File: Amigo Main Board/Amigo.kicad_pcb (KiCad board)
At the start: 2 copper layers, 75.5 x 75 mm, 39 parts, among them J1 USB_C_Receptacle_USB2.0_16P, J2 Conn_01x02, J3 SH1106 OLED, J4 MAX98357A, J5 DRV8833, J6 ButtonRibbonConnector, SW1 SW_Push, SW2 SW_Push, U1 TP4056-42-ESOP8, U2 AP2112K-3.3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

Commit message: Main PCB placement
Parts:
- added REF**: MountingHole_3.2mm_M3, MountingHole:MountingHole_3.2mm_M3, F.Cu at (15.5, 58.5)
- added REF**: MountingHole_3.2mm_M3, MountingHole:MountingHole_3.2mm_M3, F.Cu at (58.5, 15.5)
- added REF**: MountingHole_3.2mm_M3, MountingHole:MountingHole_3.2mm_M3, F.Cu at (58.5, 58.5)
- added REF**: MountingHole_3.2mm_M3, MountingHole:MountingHole_3.2mm_M3, F.Cu at (15.5, 15.5)
- moved J3 188.8 mm to (21.0, 21.7)
- moved R8 184.1 mm to (18.0, 22.5), turned to 90 degrees
- moved R9 183.7 mm to (18.0, 26.2), turned to 90 degrees
- moved J4 182.2 mm to (14.5, 22.0)
- moved C11 176.6 mm to (14.5, 41.5), turned to -90 degrees
- moved C13 175.5 mm to (24.5, 22.5), turned to -90 degrees
- moved C10 175.0 mm to (14.6, 46.0), turned to 90 degrees
- moved C12 172.2 mm to (24.5, 26.0), turned to -90 degrees
- moved U2 168.3 mm to (31.5, 22.0), turned to 180 degrees
- moved D2 168.2 mm to (37.0, 49.5)
- moved D1 166.3 mm to (37.0, 52.2)
- moved J1 165.0 mm to (22.2, 56.0)
- moved R1 164.9 mm to (25.0, 53.0)
- moved J5 164.7 mm to (27.5, 21.8)
- moved D3 164.1 mm to (56.8, 21.6), turned to 180 degrees
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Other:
- board size 75.5 x 75 mm -> 50 x 50 mm

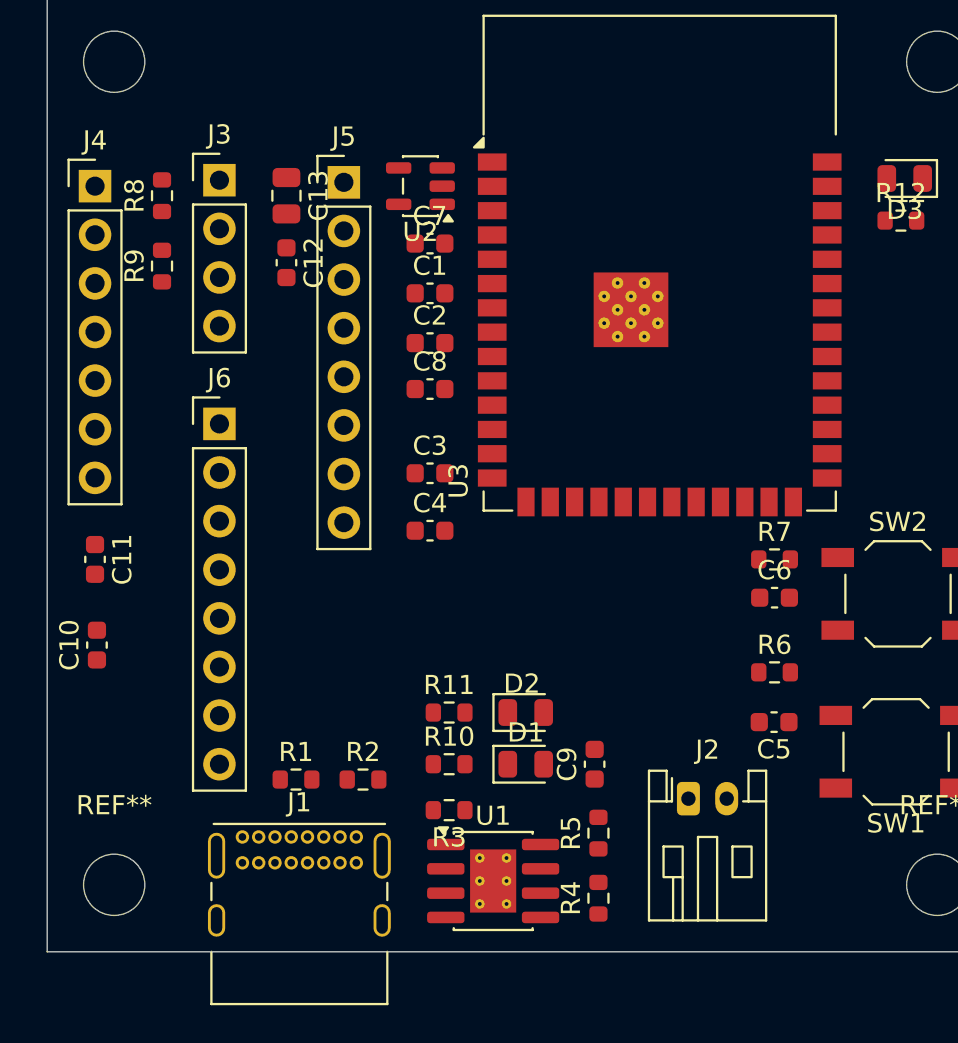
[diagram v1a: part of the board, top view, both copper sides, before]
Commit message: PCB wiring done
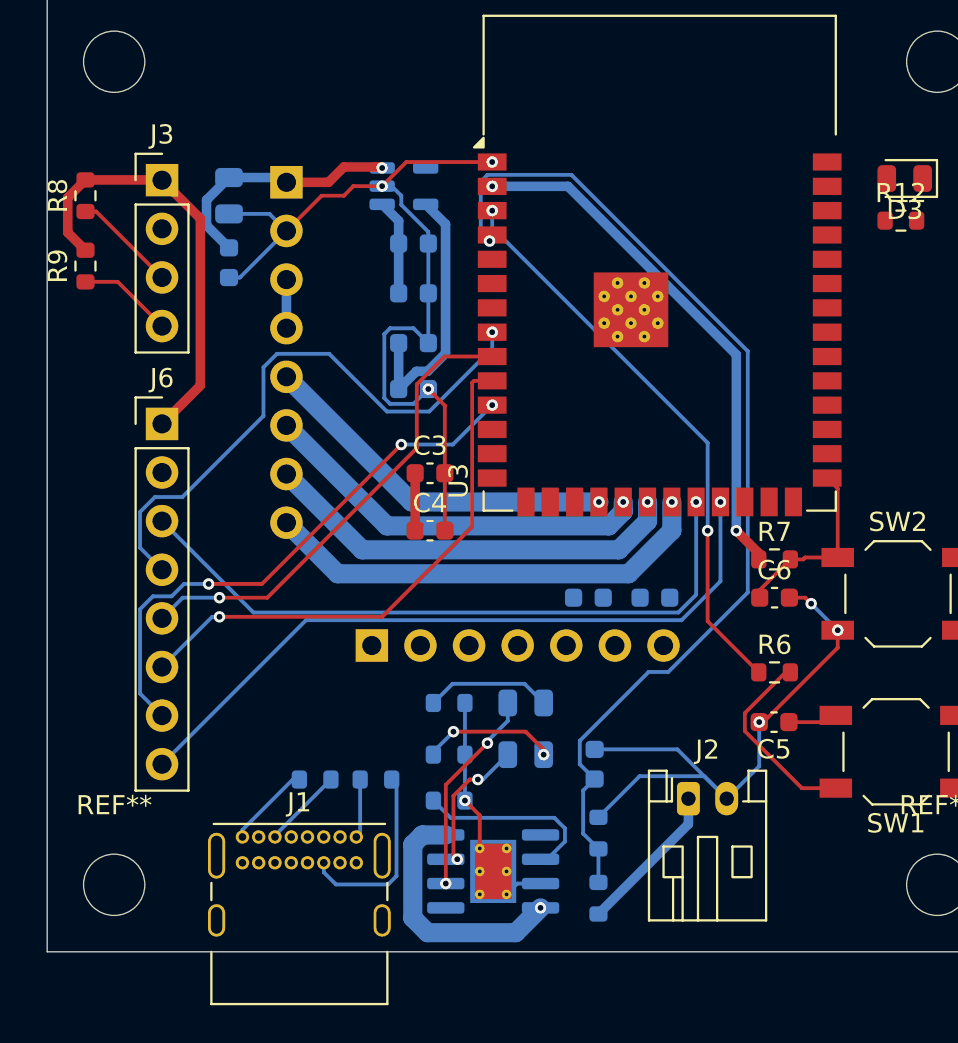
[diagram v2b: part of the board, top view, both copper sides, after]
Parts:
- C1, C10, C11, C12, C13, C2, C7, C8, C9, D1, D2, J4, J5, R1, R10, R11, R2, R3, R4, R5, U1, U2: moved to B.Cu
- moved C11 29.3 mm to (43.8, 43.5), turned to 0 degrees
- moved J4 28.0 mm to (29.0, 46.0), turned to -90 degrees
- moved C10 25.8 mm to (40.3, 43.5), turned to 180 degrees
- moved R8 4.00 mm to (14.0, 22.5)
- moved R9 4.00 mm to (14.0, 26.2)
- moved C12 3.00 mm to (21.5, 26.0)
- moved C13 3.00 mm to (21.5, 22.5)
- moved J3 3.00 mm to (18.0, 21.7)
- moved J5 3.00 mm to (24.5, 21.8), turned to 180 degrees
- moved J6 3.00 mm to (18.0, 34.4)
- moved R1 1.00 mm to (26.0, 53.0), turned to 180 degrees
- moved C1 0.86 mm to (31.1, 27.6)
- moved C2 0.86 mm to (31.1, 30.2)
- moved C7 0.86 mm to (31.1, 25.0)
- moved C8 0.86 mm to (31.1, 32.6)
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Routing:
- net GND: track 0.00 -> 93.8 mm, vias 0 -> 7
- net +3V3: track 0.00 -> 69.8 mm, vias 0 -> 2
- net BAT_SENSE: track 0.00 -> 54.1 mm, vias 0 -> 1
- net BUTTON_COL_2: track 0.00 -> 37.3 mm, vias 0 -> 1
- net BUTTON_ROW_0: track 0.00 -> 35.1 mm, vias 0 -> 1
- net BUTTON_ROW_1: track 0.00 -> 30.3 mm, vias 0 -> 1
- net EN: track 0.00 -> 29.9 mm, vias 0 -> 2
- net BUTTON_COL_1: track 0.00 -> 28.8 mm, vias 0 -> 3
- net BUTTON_COL_0: track 0.00 -> 27.9 mm, vias 0 -> 1
- net BAT+: track 0.00 -> 26.1 mm, vias 0 -> 1
- net BUTTON_ROW_2: track 0.00 -> 24.9 mm, vias 0 -> 1
- net MOTOR_B_IN2: track 0.00 -> 23.7 mm, vias 0 -> 1
- net MOTOR_B_IN1: track 0.00 -> 22.1 mm, vias 0 -> 1
- net MOTOR_A_IN2: track 0.00 -> 20.6 mm, vias 0 -> 1
- net MOTOR_A_IN1: track 0.00 -> 19.0 mm, vias 0 -> 1
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
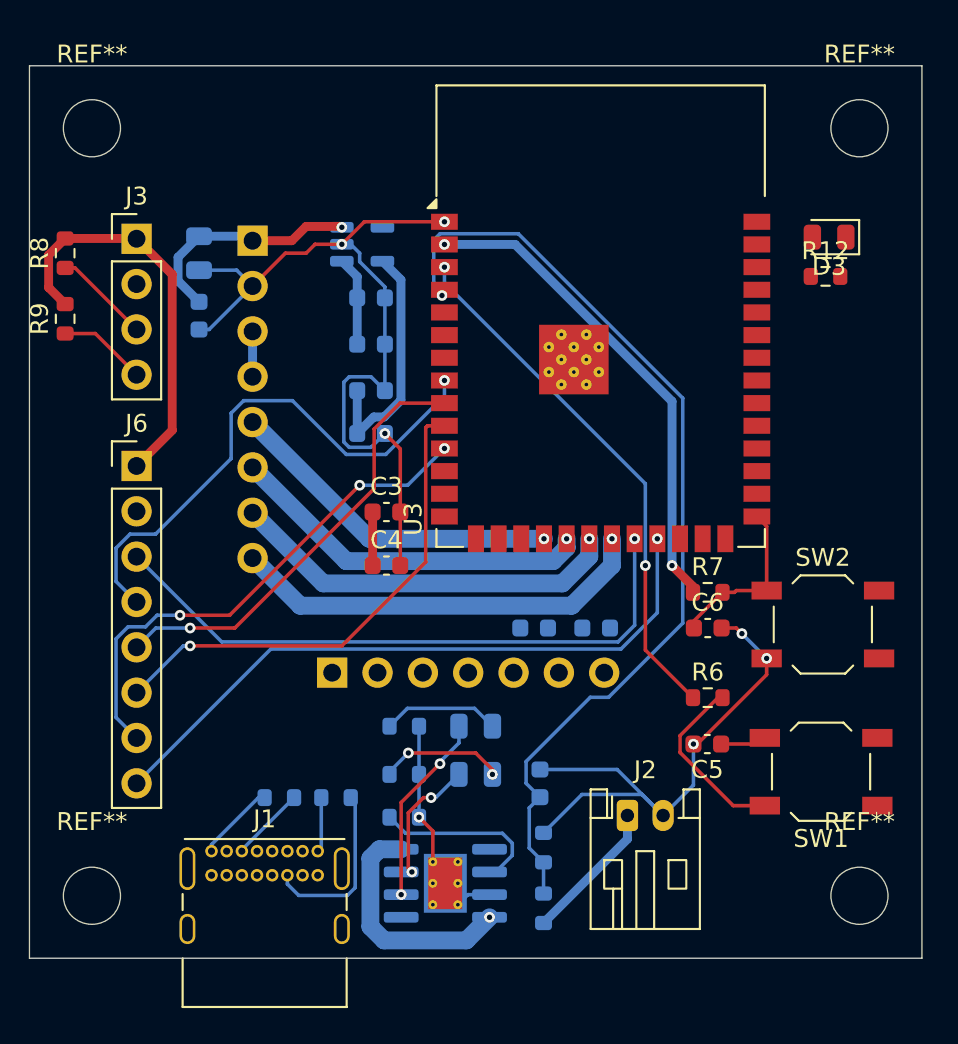
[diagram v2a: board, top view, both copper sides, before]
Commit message: Wiring first draft done. Will start the rewiring and try to avoid DRC errors
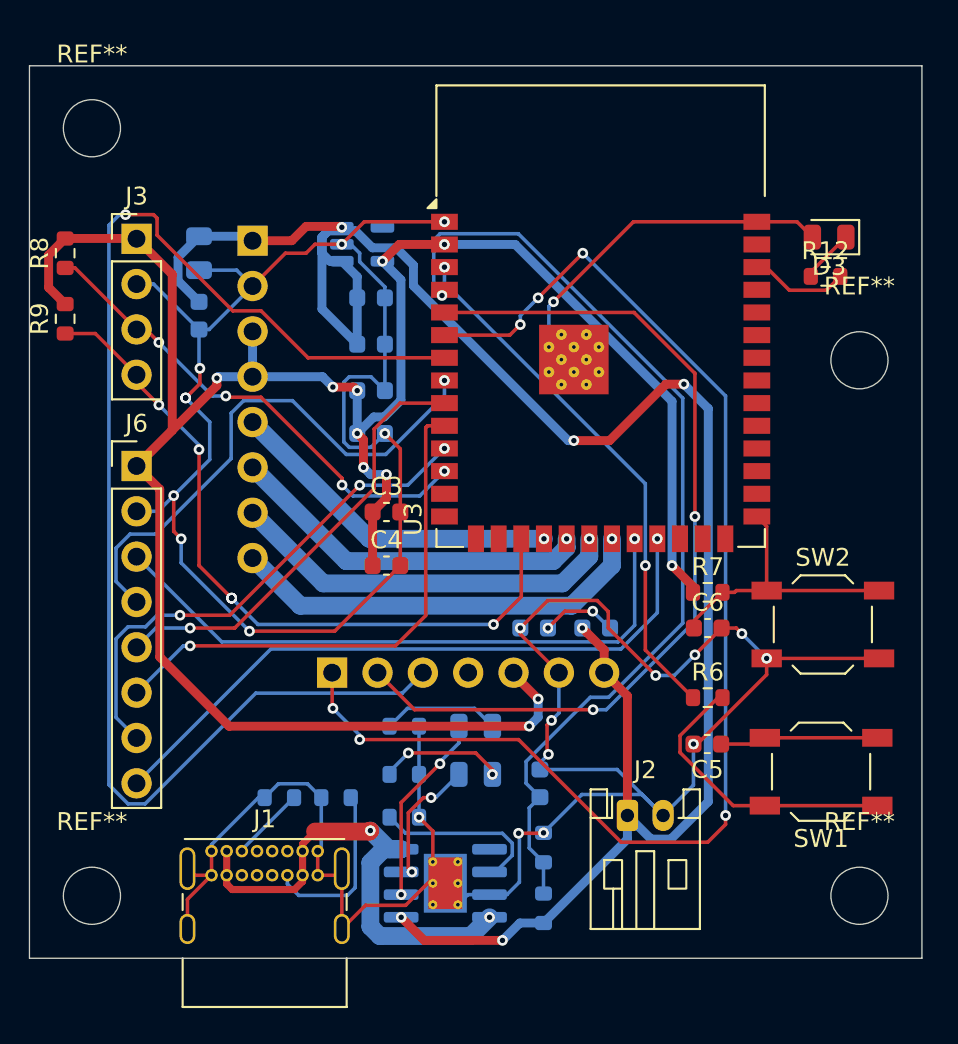
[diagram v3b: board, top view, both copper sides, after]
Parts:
- moved REF** 13.0 mm to (58.5, 28.5)
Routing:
- net GND: track 93.8 -> 211.2 mm, vias 7 -> 21
- net BAT+: track 26.1 -> 114.1 mm, vias 1 -> 6
- net AUDIO_DOUT: track 0.00 -> 75.3 mm, vias 0 -> 1
- net AUDIO_LRC_WS: track 0.00 -> 72.9 mm, vias 0 -> 6
- net +3V3: track 69.8 -> 131.9 mm, vias 2 -> 11
- net AUDIO_BCLK: track 0.00 -> 50.0 mm, vias 0 -> 2
- net OLED_SCL: track 4.96 -> 40.4 mm, vias 0 -> 6
- net OLED_SDA: track 5.43 -> 27.3 mm, vias 0 -> 4
- net VBUS_5V: track 13.3 -> 27.7 mm, vias 1 -> 2
- net IO0: track 9.56 -> 15.9 mm
- net Net-(R6-Pad2): track 10.2 -> 16.5 mm
- net Net-(C5-Pad1): track 2.59 -> 8.89 mm
- net LED_STATUS: track 0.00 -> 5.53 mm
- net Net-(C10-Pad1): track 0.00 -> 4.26 mm, vias 0 -> 2
- net Net-(D3-K): track 0.00 -> 3.01 mm
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
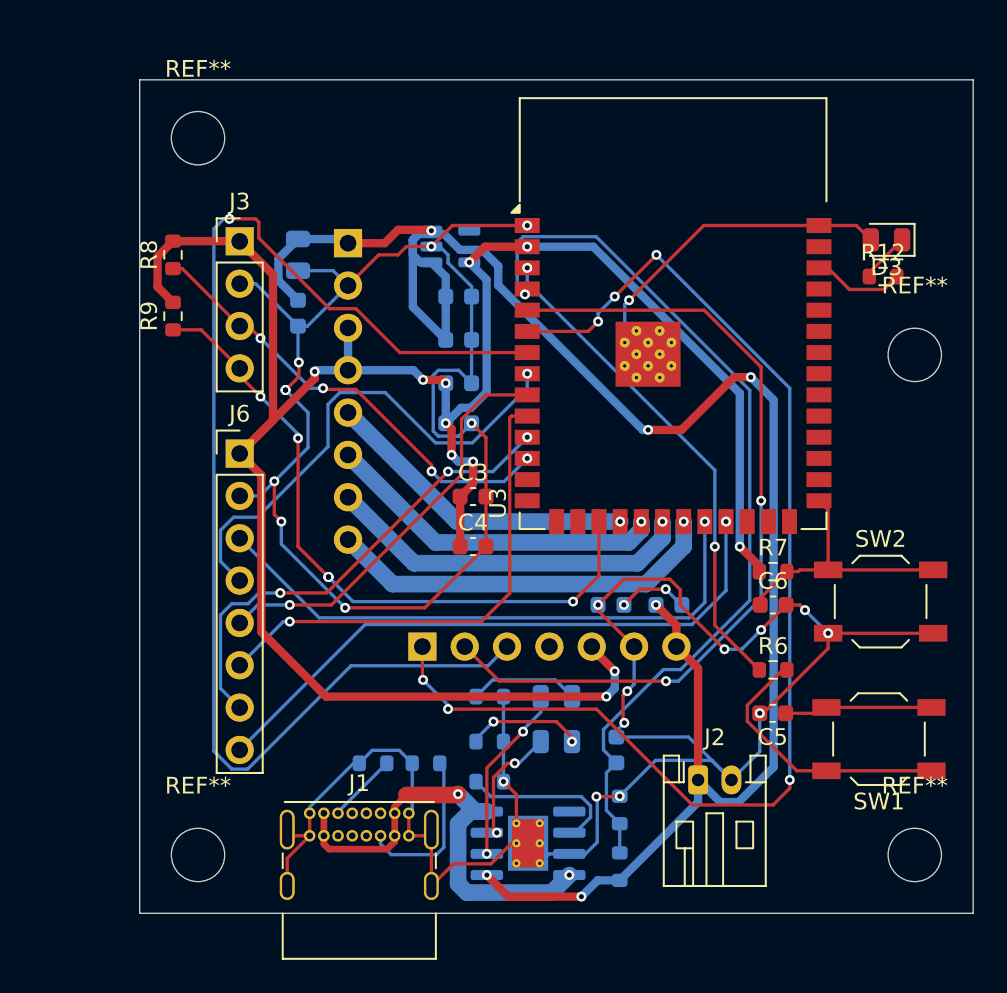
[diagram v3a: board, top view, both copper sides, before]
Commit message: Positioned Everything
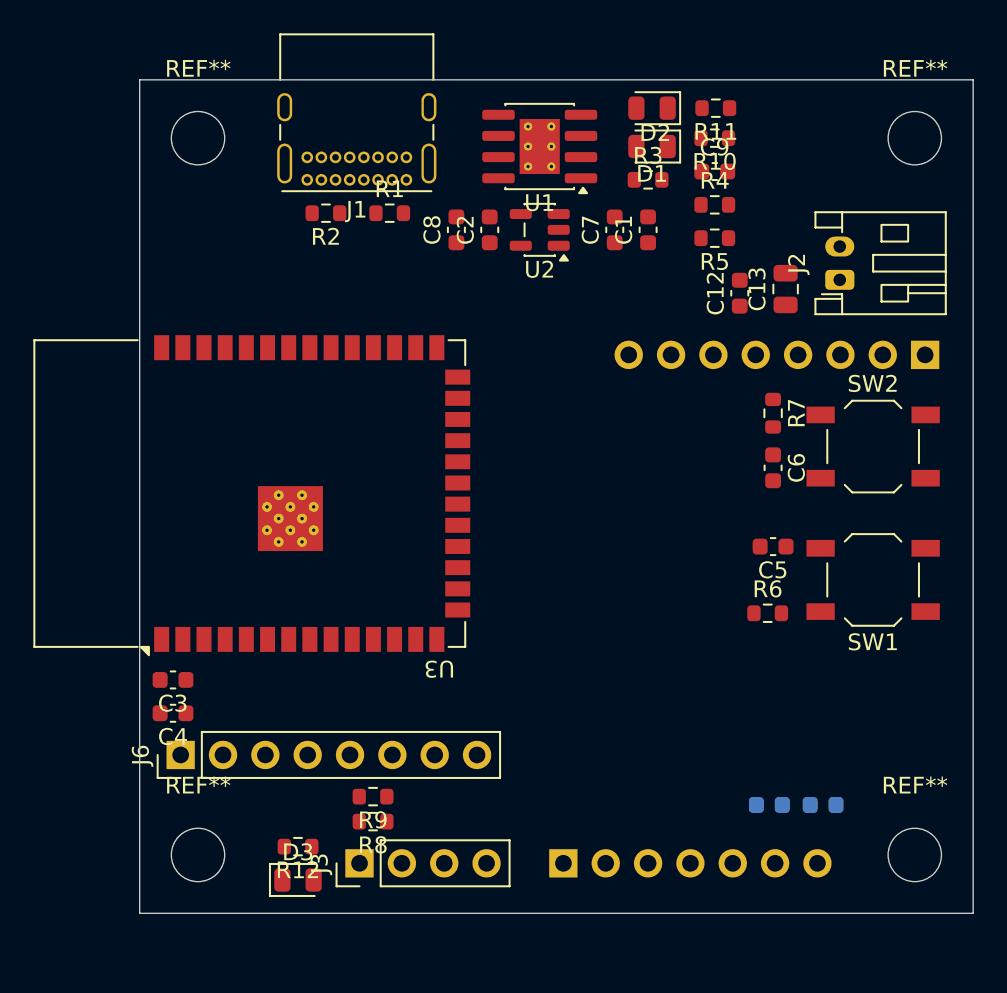
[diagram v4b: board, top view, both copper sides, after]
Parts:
- C1, C12, C13, C2, C7, C8, C9, D1, D2, R1, R10, R11, R2, R3, R4, R5, U1, U2: moved to F.Cu
- moved D3 52.2 mm to (21.5, 60.0), turned to 0 degrees
- moved R12 49.0 mm to (21.5, 58.0), turned to 180 degrees
- moved U1 41.8 mm to (36.0, 16.0)
- moved R4 40.1 mm to (46.5, 19.5), turned to 0 degrees
- moved R10 38.6 mm to (46.5, 15.5)
- moved J1 38.4 mm to (28.0, 18.0), turned to 180 degrees
- moved J3 38.0 mm to (25.2, 59.0), turned to 90 degrees
- moved R11 37.8 mm to (46.6, 13.7)
- moved R3 37.3 mm to (42.5, 18.0)
- moved D1 36.2 mm to (42.7, 16.0)
- moved R8 36.1 mm to (26.0, 56.5), turned to 180 degrees
- moved D2 35.8 mm to (42.7, 13.7)
- moved J5 35.3 mm to (59.1, 28.5), turned to 90 degrees
- moved C9 35.2 mm to (46.5, 17.5), turned to 0 degrees
- moved R5 34.8 mm to (46.5, 21.5), turned to 180 degrees
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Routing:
- net GND: track 211.2 -> 0.00 mm, vias 21 -> 0
- net +3V3: track 131.9 -> 0.00 mm, vias 11 -> 0
- net BAT+: track 114.1 -> 0.00 mm, vias 6 -> 0
- net AUDIO_DOUT: track 75.3 -> 0.00 mm, vias 1 -> 0
- net AUDIO_LRC_WS: track 72.9 -> 0.00 mm, vias 6 -> 0
- net BAT_SENSE: track 54.1 -> 0.00 mm, vias 1 -> 0
- net AUDIO_BCLK: track 50.0 -> 0.00 mm, vias 2 -> 0
- net OLED_SCL: track 40.4 -> 0.00 mm, vias 6 -> 0
- net BUTTON_COL_2: track 37.3 -> 0.00 mm, vias 1 -> 0
- net BUTTON_ROW_0: track 35.1 -> 0.00 mm, vias 1 -> 0
- net BUTTON_ROW_1: track 30.3 -> 0.00 mm, vias 1 -> 0
- net EN: track 29.9 -> 0.00 mm, vias 2 -> 0
- net BUTTON_COL_0: track 29.6 -> 0.00 mm, vias 1 -> 0
- net BUTTON_COL_1: track 28.8 -> 0.00 mm, vias 3 -> 0
- net VBUS_5V: track 27.7 -> 0.00 mm, vias 2 -> 0
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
